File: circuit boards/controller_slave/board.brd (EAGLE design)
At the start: 75.1 x 52.5 mm, 65 parts, among them IC1 74HC595D, IC2 74HC595D, IC3 74HC595D, IC4 7805TV, Q1 14,7456

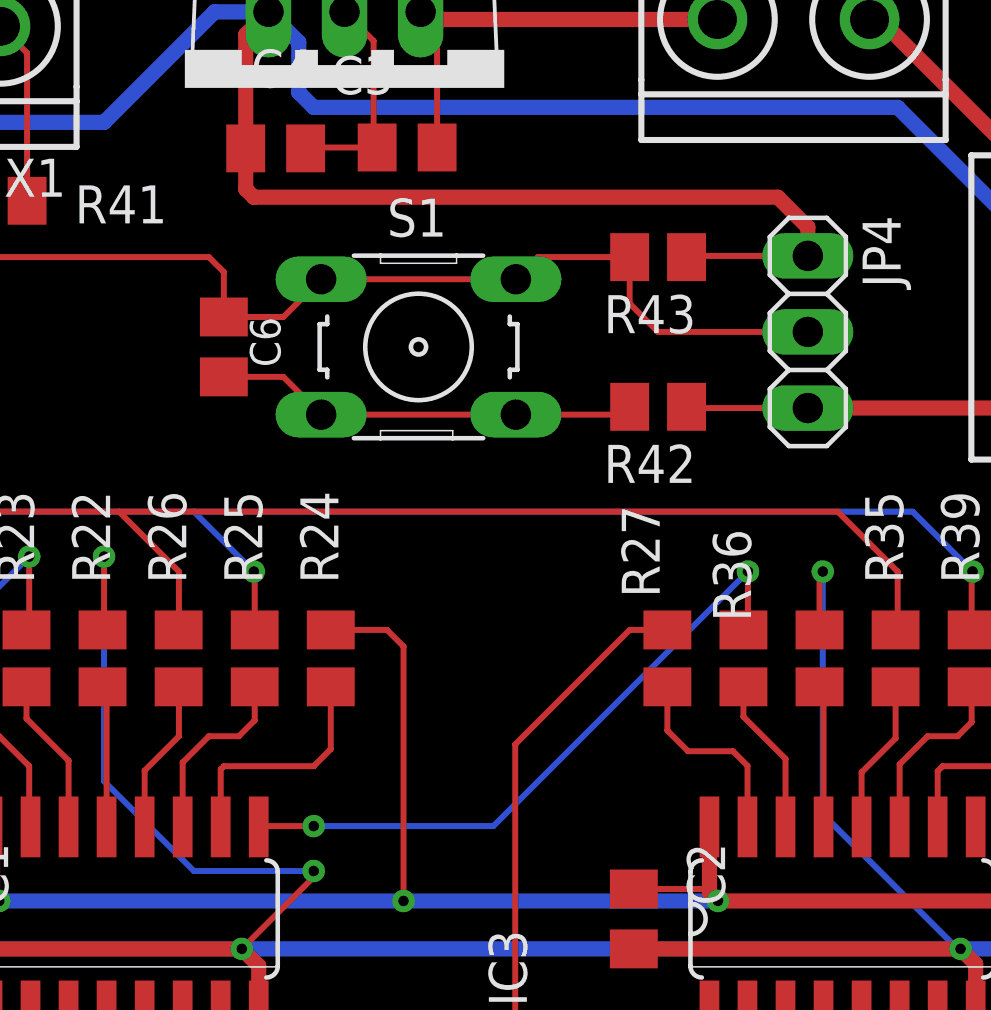
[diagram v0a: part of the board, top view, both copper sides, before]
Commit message: removed reset circuit from board design
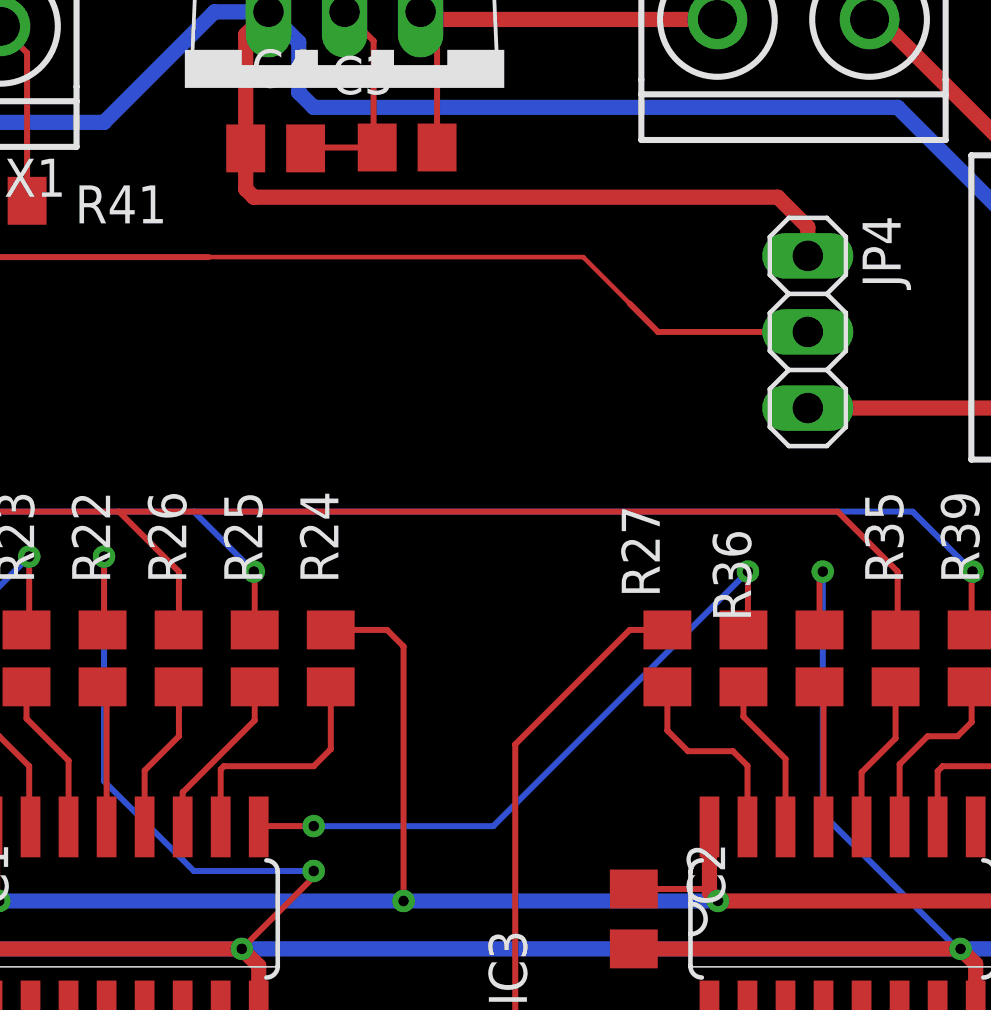
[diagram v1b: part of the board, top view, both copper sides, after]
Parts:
- removed C6: 4,7nF, rcl:C0805K
- removed R42: 1K, resistor:M0805
- removed R43: 10K, resistor:M0805
- removed S1: (no value), switch-omron:B3F-10XX
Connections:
- removed net N$76: C6.2, R42.2, S1.3, S1.4
- net +5V: no longer R43.1
- net GND: no longer R42.1
- net N$75: no longer C6.1, R43.2, S1.1, S1.2
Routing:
- net N$76: track 14.2 -> 0.00 mm
- net GND: track 276.6 -> 272.5 mm
- net +5V: track 215.7 -> 211.7 mm
- net N$75: track 42.9 -> 39.5 mm
- net N$32: track 6.26 -> 5.67 mm
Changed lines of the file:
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@@
 <drawing>
 <settings>
-<setting alwaysvectorfont="yes"/>
+<setting alwaysvectorfont="no"/>
 <setting verticaltext="up"/>
 </settings>
@@
 <attribute name="VALUE" x="57.325" y="40.31" size="1.27" layer="27" rot="R270"/>
 </element>
-<element name="C6" library="rcl" library_urn="urn:adsk.eagle:library:334" package="C0805K" package3d_urn="urn:adsk.eagle:package:23681/2" value="4,7nF" x="41" y="36" smashed="yes" rot="R270">
-<attribute name="NAME" x="41.875" y="37" size="1.016" layer="25" rot="R270"/>
-<attribute name="POPULARITY" value="52" x="41" y="36" size="1.778" layer="27" rot="R270" display="off"/>
-<attribute name="SPICEPREFIX" value="C" x="41" y="36" size="1.778" layer="27" rot="R270" display="off"/>
-<attribute name="VALUE" x="38.6" y="37" size="1.016" layer="27" rot="R270"/>
-</element>
-<element name="R42" library="resistor" library_urn="urn:adsk.eagle:library:348" package="M0805" value="1K" x="55.5" y="34" smashed="yes" rot="R180">
-<attribute name="NAME" x="56.77" y="32.73" size="1.27" layer="25" rot="R180"/>
-<attribute name="VALUE" x="56.77" y="32.54" size="1.27" layer="27" rot="R180"/>
-</element>
-<element name="R43" library="resistor" library_urn="urn:adsk.eagle:library:348" package="M0805" value="10K" x="55.5" y="39" smashed="yes" rot="R180">
-<attribute name="NAME" x="56.77" y="37.73" size="1.27" layer="25" rot="R180"/>
-<attribute name="VALUE" x="56.77" y="37.54" size="1.27" layer="27" rot="R180"/>
-</element>
-<element name="S1" library="switch-omron" library_urn="urn:adsk.eagle:library:377" package="B3F-10XX" package3d_urn="urn:adsk.eagle:package:27496/1" value="" x="47.5" y="36" smashed="yes">
-<attribute name="MF" value="" x="47.5" y="36" size="1.778" layer="27" display="off"/>
-<attribute name="MPN" value="B3F-1000" x="47.5" y="36" size="1.778" layer="27" display="off"/>
-<attribute name="NAME" x="46.452" y="39.683" size="1.27" layer="25" ratio="10"/>
-<attribute name="OC_FARNELL" value="176432" x="47.5" y="36" size="1.778" layer="27" display="off"/>
-<attribute name="OC_NEWARK" value="36M3542" x="47.5" y="36" size="1.778" layer="27" display="off"/>
-<attribute name="POPULARITY" value="72" x="47.5" y="36" size="1.778" layer="27" display="off"/>
-<attribute name="VALUE" x="44.452" y="30.92" size="1.27" layer="27" ratio="10"/>
-</element>
 </elements>
 <signals>
@@
 <wire x1="69.985" y1="39.8589" x2="69.985" y2="34.7789" width="0.508" layer="1"/>
 <contactref element="JP4" pad="3"/>
-<contactref element="R42" pad="1"/>
 <wire x1="17.6" y1="15.9" x2="9.1" y2="15.9" width="0.2" layer="1"/>
 <wire x1="9.1" y1="15.9" x2="8" y2="17" width="0.2" layer="1"/>
@@
 <wire x1="23.5" y1="49" x2="24.5" y2="48" width="0.2" layer="1"/>
 <wire x1="13" y1="49" x2="23.5" y2="49" width="0.2" layer="1"/>
-<wire x1="60.5" y1="33.96" x2="56.49" y2="33.96" width="0.2" layer="1"/>
-<wire x1="56.49" y1="33.96" x2="56.45" y2="34" width="0.2" layer="1"/>
 <wire x1="60.5" y1="33.96" x2="69.1661" y2="33.96" width="0.508" layer="1"/>
 <wire x1="69.1661" y1="33.96" x2="69.985" y2="34.7789" width="0.508" layer="1"/>
@@
 <via x="67.5" y="17.5" extent="1-16" drill="0.35"/>
 <contactref element="JP4" pad="1"/>
-<contactref element="R43" pad="1"/>
 <wire x1="9.5" y1="17.5" x2="8.1" y2="18.9" width="0.2" layer="1"/>
 <wire x1="8.1" y1="18.9" x2="6.81" y2="18.9" width="0.2" layer="1"/>
@@
 <wire x1="60.5" y1="40" x2="60.5" y2="39.04" width="0.508" layer="1"/>
 <wire x1="42" y1="41" x2="59.5" y2="41" width="0.508" layer="1"/>
-<wire x1="56.45" y1="39" x2="56.49" y2="39.04" width="0.2" layer="1"/>
-<wire x1="56.49" y1="39.04" x2="60.5" y2="39.04" width="0.2" layer="1"/>
 </signal>
 <signal name="N$10">
@@
 <contactref element="R25" pad="2"/>
 <contactref element="IC1" pad="11"/>
-<wire x1="39.625" y1="19.9734" x2="39.625" y2="22.125" width="0.2" layer="1"/>
+<wire x1="39.625" y1="19.9734" x2="39.625" y2="21.125" width="0.2" layer="1"/>
 <wire x1="42.03" y1="23.53" x2="42.03" y2="24.65" width="0.2" layer="1"/>
-<wire x1="39.625" y1="22.125" x2="40.5" y2="23" width="0.2" layer="1"/>
-<wire x1="40.5" y1="23" x2="41.5" y2="23" width="0.2" layer="1"/>
-<wire x1="41.5" y1="23" x2="42.03" y2="23.53" width="0.2" layer="1"/>
+<wire x1="39.625" y1="21.125" x2="42.03" y2="23.53" width="0.2" layer="1"/>
 </signal>
 <signal name="N$33">
@@
 </signal>
 <signal name="N$75">
-<contactref element="S1" pad="1"/>
-<contactref element="R43" pad="2"/>
-<contactref element="C6" pad="1"/>
-<contactref element="S1" pad="2"/>
 <contactref element="JP4" pad="2"/>
 <contactref element="U$1" pad="16"/>
-<wire x1="41" y1="37" x2="42.9882" y2="37" width="0.2" layer="1"/>
-<wire x1="42.9882" y1="37" x2="44.2488" y2="38.2606" width="0.2" layer="1"/>
-<wire x1="44.2488" y1="38.2606" x2="50.7512" y2="38.2606" width="0.2" layer="1"/>
-<wire x1="50.7512" y1="38.2606" x2="51.4906" y2="39" width="0.2" layer="1"/>
-<wire x1="51.4906" y1="39" x2="54.55" y2="39" width="0.2" layer="1"/>
-<wire x1="54.55" y1="39" x2="54.55" y2="37.45" width="0.2" layer="1"/>
 <wire x1="54.55" y1="37.45" x2="55.5" y2="36.5" width="0.2" layer="1"/>
 <wire x1="55.5" y1="36.5" x2="60.5" y2="36.5" width="0.2" layer="1"/>
 <wire x1="22.8942" y1="41" x2="24" y2="41" width="0.2" layer="1"/>
-<wire x1="40.5" y1="39" x2="41" y2="38.5" width="0.2" layer="1"/>
-<wire x1="41" y1="38.5" x2="41" y2="37" width="0.2" layer="1"/>
 <wire x1="24" y1="41" x2="26" y2="39" width="0.2" layer="1"/>
 <wire x1="26" y1="39" x2="40.5" y2="39" width="0.2" layer="1"/>
-</signal>
-<signal name="N$76">
-<contactref element="R42" pad="2"/>
-<contactref element="C6" pad="2"/>
-<contactref element="S1" pad="3"/>
-<contactref element="S1" pad="4"/>
-<wire x1="44.2488" y1="33.7394" x2="50.7512" y2="33.7394" width="0.2" layer="1"/>
-<wire x1="50.7512" y1="33.7394" x2="54.2894" y2="33.7394" width="0.2" layer="1"/>
-<wire x1="54.2894" y1="33.7394" x2="54.55" y2="34" width="0.2" layer="1"/>
-<wire x1="41" y1="35" x2="42.9882" y2="35" width="0.2" layer="1"/>
-<wire x1="42.9882" y1="35" x2="44.2488" y2="33.7394" width="0.2" layer="1"/>
+<wire x1="40.5" y1="39" x2="53" y2="39" width="0.1524" layer="1"/>
+<wire x1="53" y1="39" x2="54.55" y2="37.45" width="0.1524" layer="1"/>
 </signal>
 </signals>
